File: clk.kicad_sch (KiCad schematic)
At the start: 26 parts, among them U7 SY75602BTWL-TR, U8 SI5338B-B-GM, U9 LMK1C1102DQFT

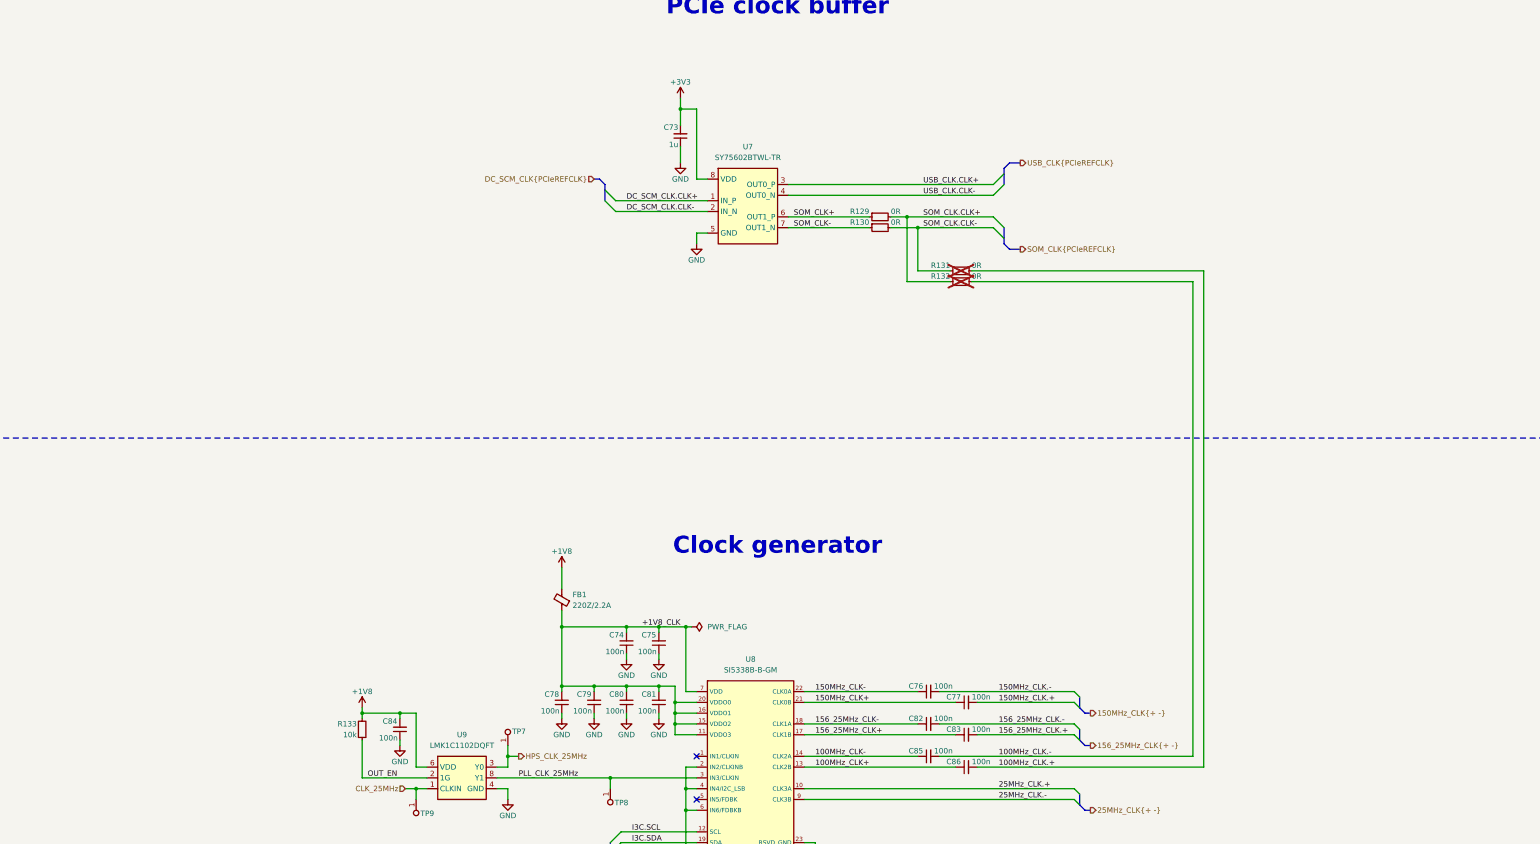
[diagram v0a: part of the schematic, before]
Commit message: [#100687] Reroute PCIE clocks
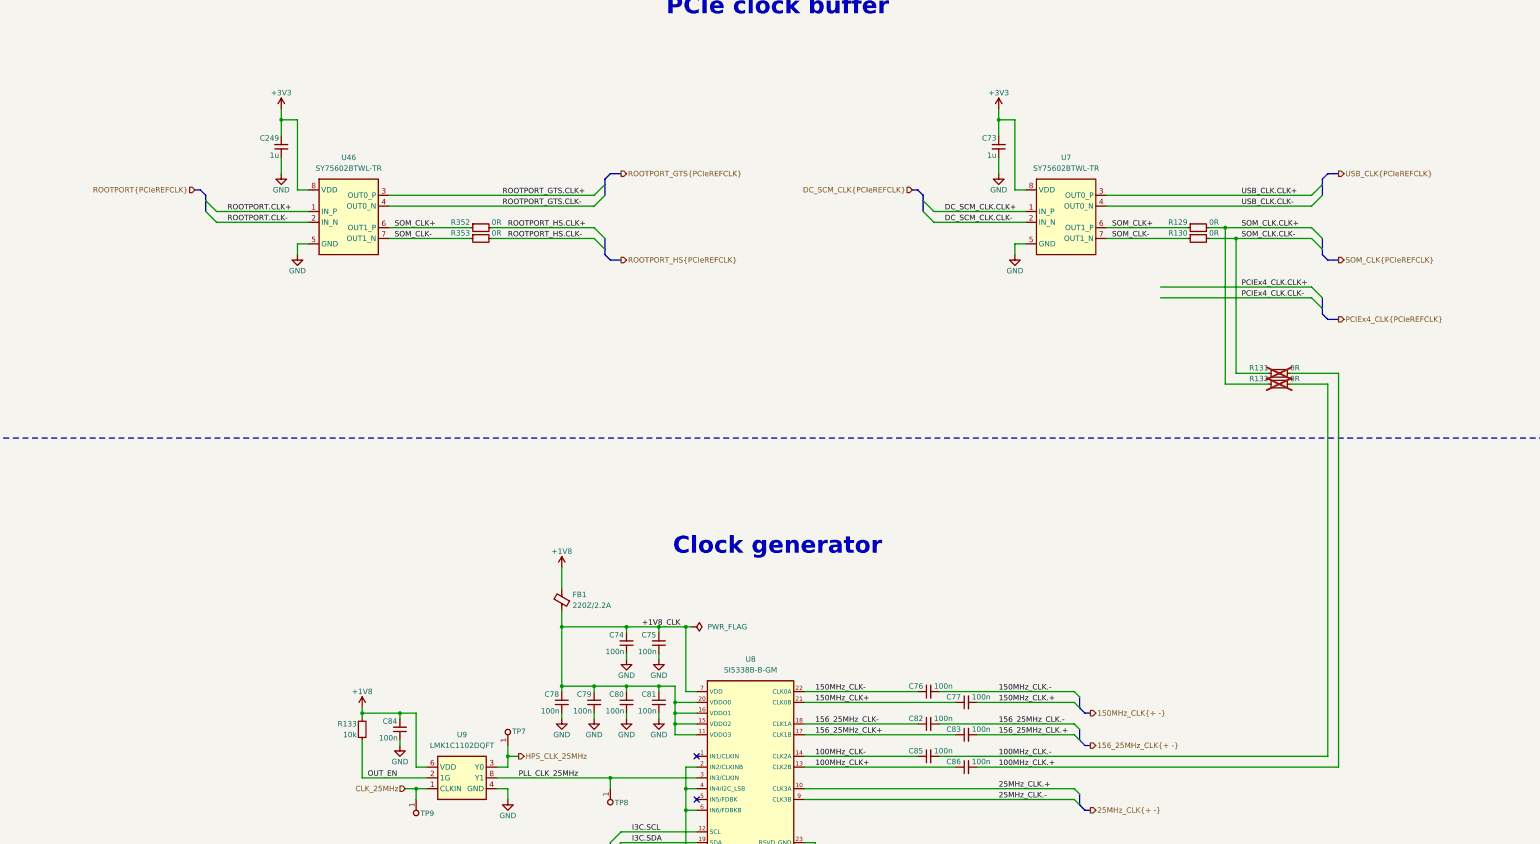
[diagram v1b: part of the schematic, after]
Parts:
- added C249: C_1u_25V_0402, antmicro-footprints:C_0402_1005Metric, symbol antmicroCapacitors0402:C_1u_25V_0402
- added R352, R353: R_0R_0402, antmicro-footprints:R_0402_1005Metric, symbol antmicroResistors0402:R_0R_0402
- added U46: SY75602BTWL-TR, antmicro-footprints:VDFN-8_1.6x1.4mm_P0.4mm, symbol antmicroClockTimingClockGeneratorsPLLsFrequencySynthesizers:SY75602BTWL-TR
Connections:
- net +3V3: now also C249.2, U46.8 (VDD)
- net GND: now also C249.1, U46.5 (GND)
- net SOM_CLK+: now also R352.1, U46.6 (OUT1_P)
- net SOM_CLK-: now also R353.1, U46.7 (OUT1_N)
- new net ROOTPORT.CLK+: U46.1 (IN_P)
- new net ROOTPORT.CLK-: U46.2 (IN_N)
- new net ROOTPORT_GTS.CLK+: U46.3 (OUT0_P)
- new net ROOTPORT_GTS.CLK-: U46.4 (OUT0_N)
- new net ROOTPORT_HS.CLK+: R352.2
- new net ROOTPORT_HS.CLK-: R353.2
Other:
- moved on the sheet: C73, R129, R130, R131, R132, U7

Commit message: [#100687] Add clocks
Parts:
- added C250: C_1u_25V_0402, antmicro-footprints:C_0402_1005Metric, symbol antmicroCapacitors0402:C_1u_25V_0402
- added C251: C_100n_0402, antmicro-footprints:C_0402_1005Metric, symbol antmicroCapacitors0402:C_100n_0402
- added R354, R355, R356, R357, R358, R359: R_0R_0402, antmicro-footprints:R_0402_1005Metric, symbol antmicroResistors0402:R_0R_0402
- added U47: DSC557-0344FI0T, antmicro-footprints:VQFN-14-1EP_3.2x2.5mm_P0.5mm_Layout4x3, symbol antmicroClockTimingRealTimeClocks:DSC557-0344FI0T
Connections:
- net +3V3: now also C250.2, C251.2, U47.1 (OE), U47.12 (VDD1), U47.13 (VDD0)
- net GND: now also C250.1, C251.1, U47.15 (EPAD), U47.4 (VSS)
- net ROOTPORT_GTS.CLK+: now also R354.2, R356.2; no longer U46.3 (OUT0_P)
- net ROOTPORT_GTS.CLK-: now also R355.2, R357.2; no longer U46.4 (OUT0_N)
- net ROOTPORT_HS.CLK+: now also R358.2
- net ROOTPORT_HS.CLK-: now also R359.2
- net SOM_CLK+: no longer R352.1, U46.6 (OUT1_P)
- net SOM_CLK-: no longer R353.1, U46.7 (OUT1_N)
- new net: R356.1, U47.11 (CLK0+)
- new net: R354.1, U46.3 (OUT0_P)
- new net: R352.1, U46.6 (OUT1_P)
- new net: R359.1, U47.9 (CLK1-)
- new net: R357.1, U47.10 (CLK0-)
- new net: U47.14 (NC), U47.2 (NC), U47.3 (NC), U47.5 (NC), U47.6 (NC), U47.7 (NC)
- new net: R358.1, U47.8 (CLK1+)
- new net: R355.1, U46.4 (OUT0_N)
- new net: R353.1, U46.7 (OUT1_N)
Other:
- moved on the sheet: R352, R353

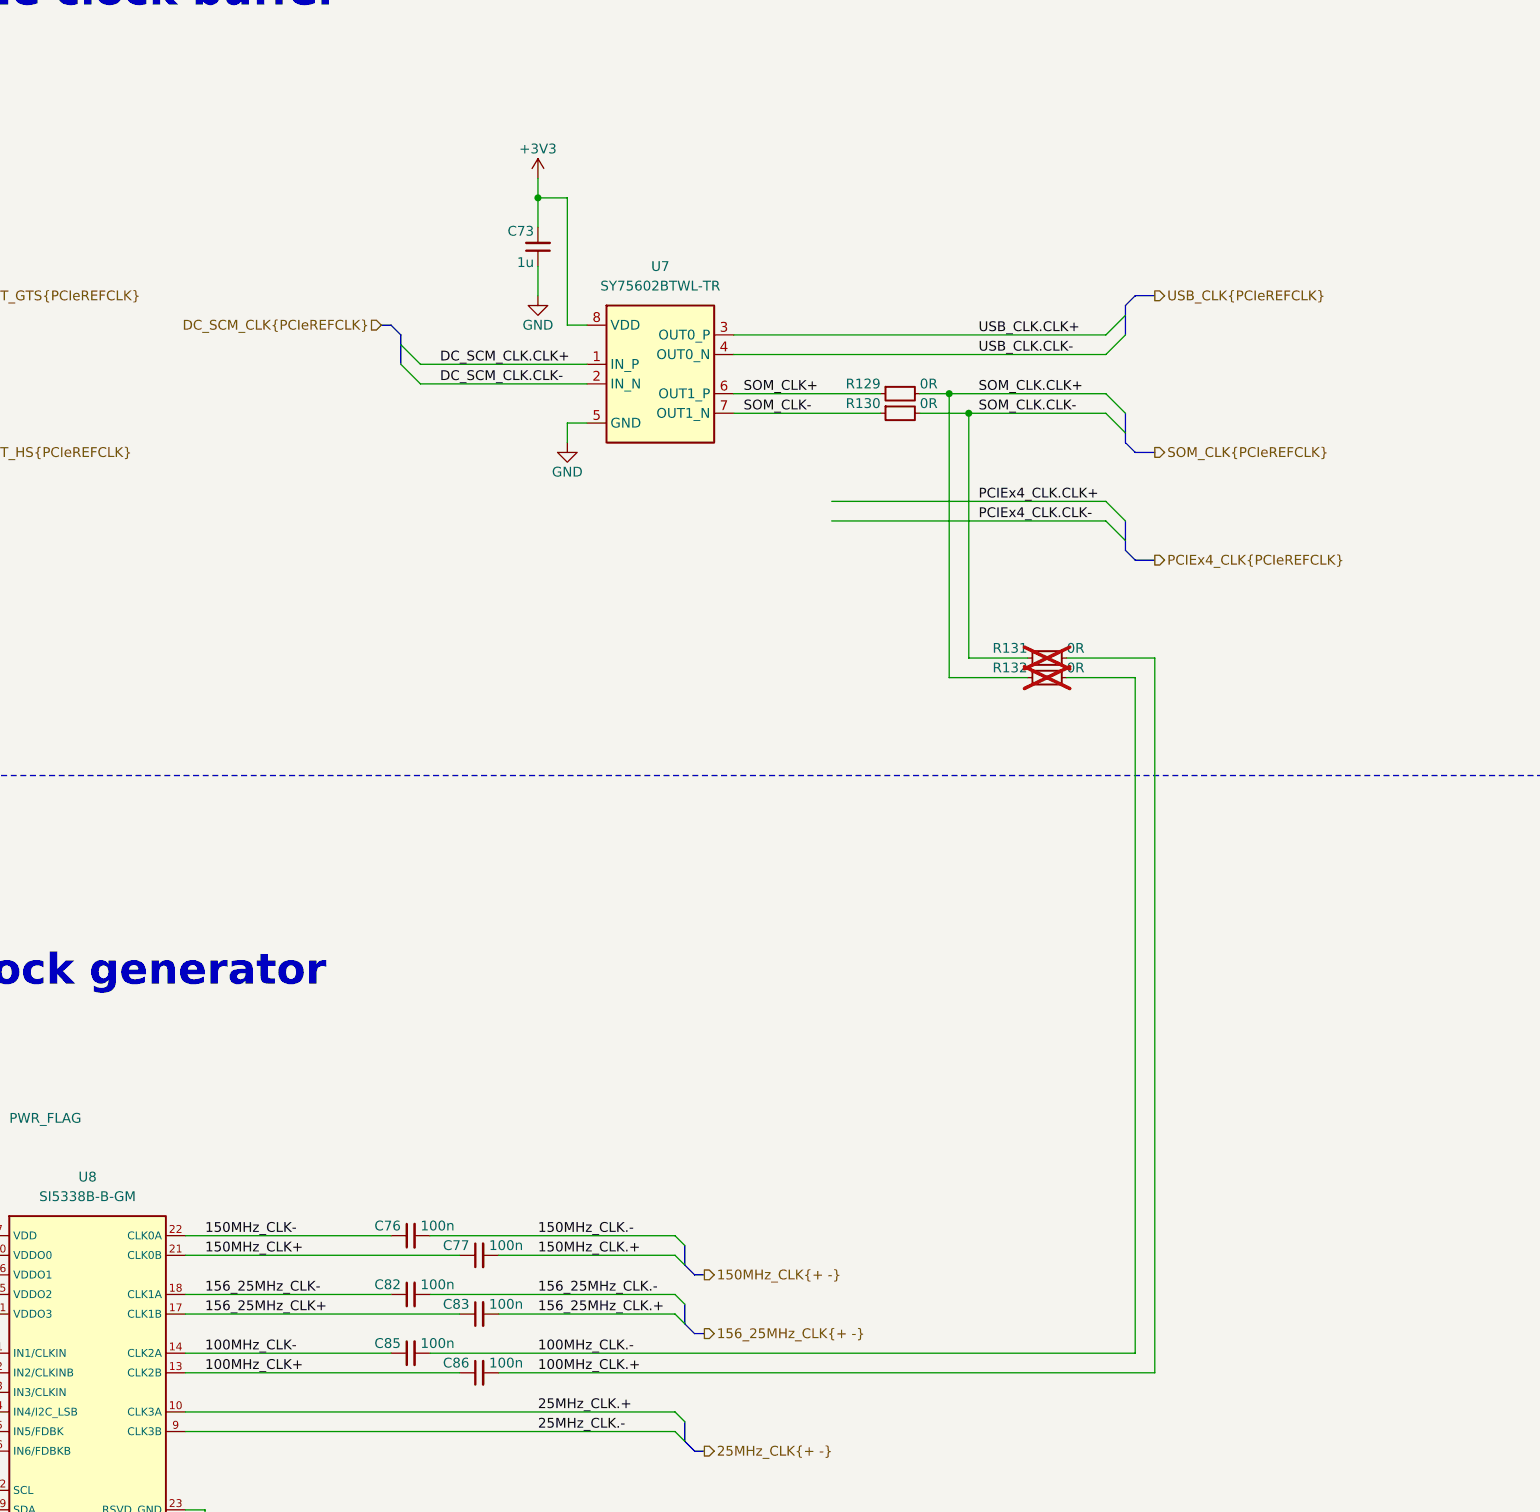
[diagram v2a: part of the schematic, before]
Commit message: [#100687] Update LDO and CLK
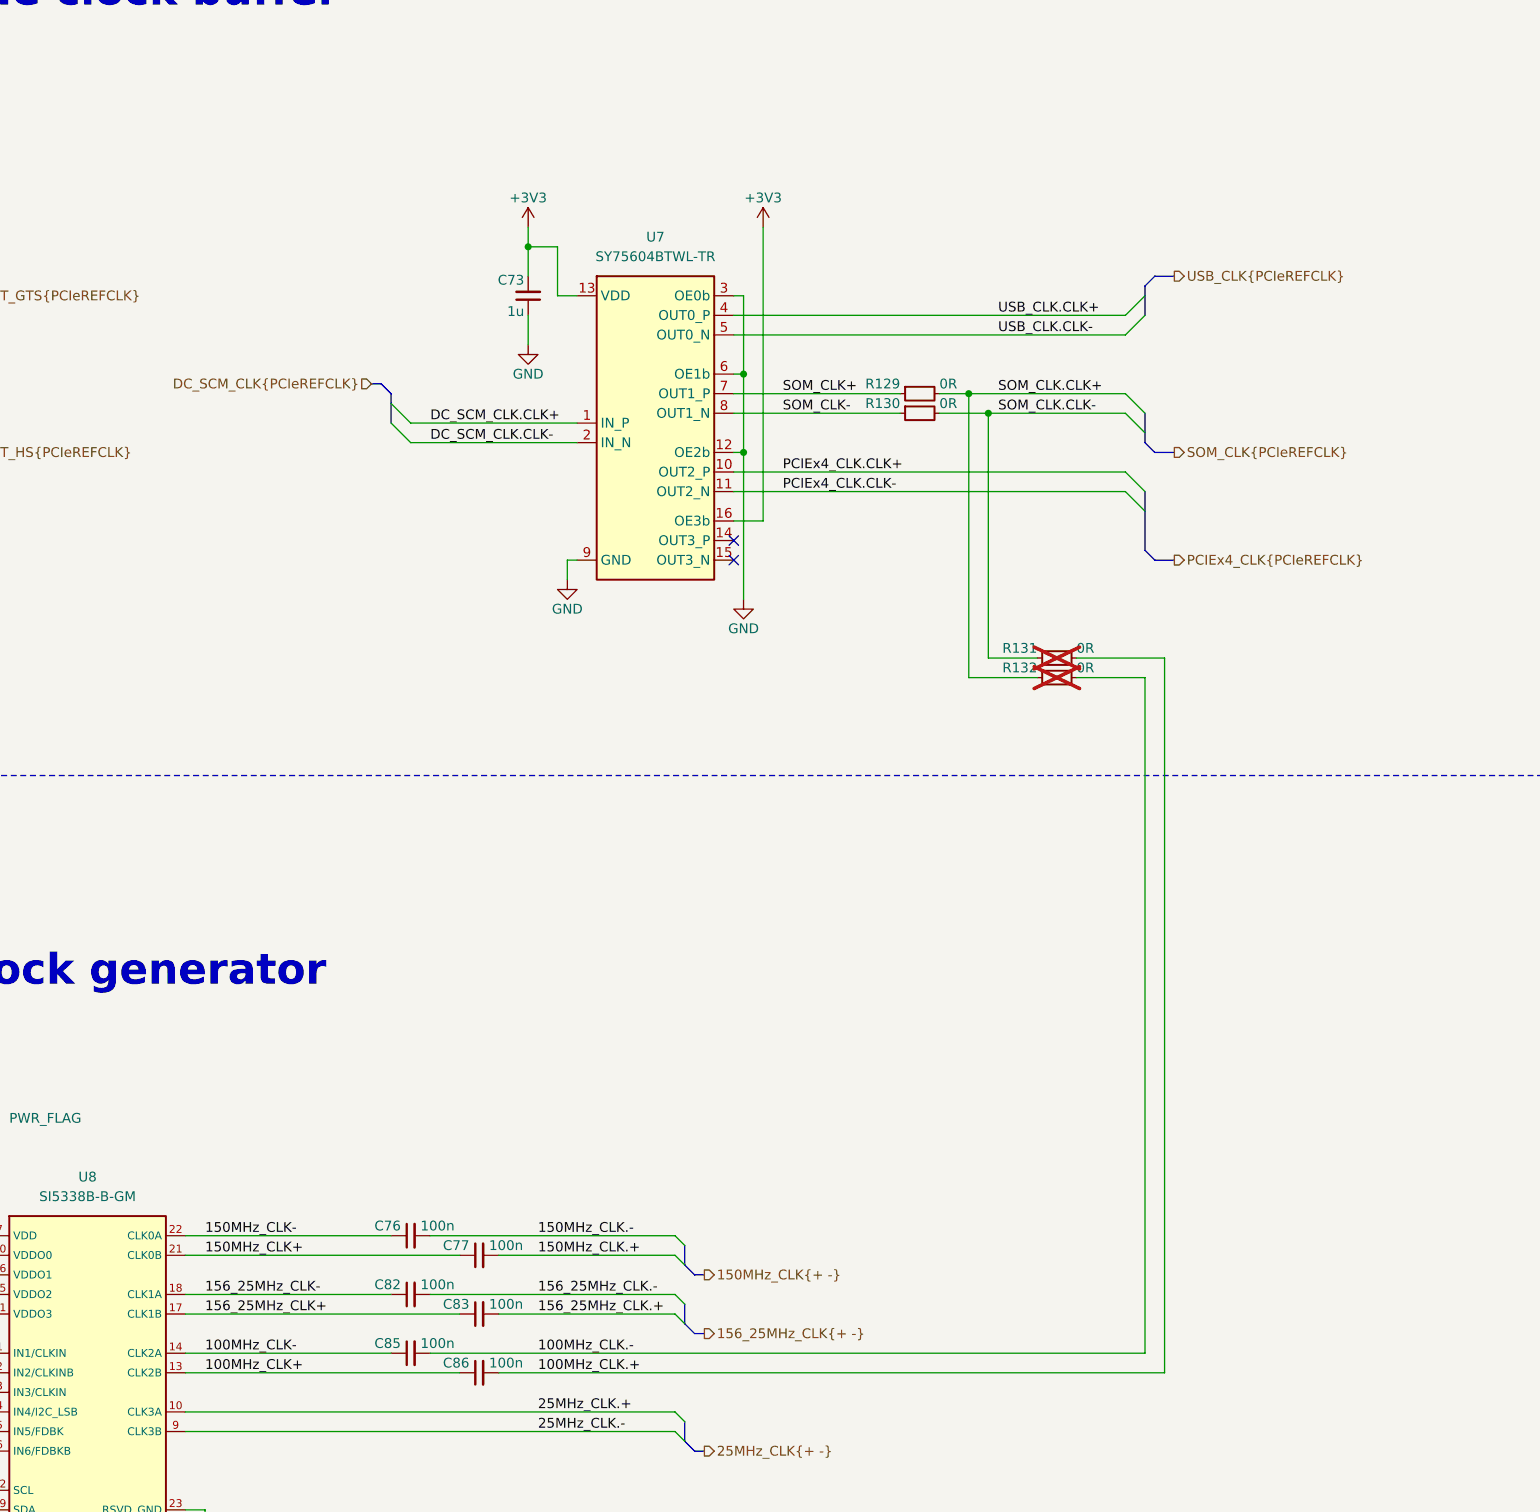
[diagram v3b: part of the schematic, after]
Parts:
- removed U7: SY75602BTWL-TR, antmicro-footprints:VDFN-8_1.6x1.4mm_P0.4mm, symbol antmicroClockTimingClockGeneratorsPLLsFrequencySynthesizers:SY75602BTWL-TR
- added U7: SY75604BTWL-TR, antmicro-footprints:VQFN-16-1EP_3x3mm_P0.5mm_EP1.68x1.68mm, symbol antmicroClockTimingClockGeneratorsPLLsFrequencySynthesizers:SY75604BTWL-TR_1
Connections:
- net +3V3: now also U7.13 (VDD), U7.16 (OE3b)
- net DC_SCM_CLK.CLK+: now also U7.1 (IN_P)
- net DC_SCM_CLK.CLK-: now also U7.2 (IN_N)
- net GND: now also U7.12 (OE2b), U7.3 (OE0b), U7.6 (OE1b), U7.9 (GND)
- net PCIEx4_CLK.CLK+: now also U7.10 (OUT2_P)
- net PCIEx4_CLK.CLK-: now also U7.11 (OUT2_N)
- net SOM_CLK+: now also U7.7 (OUT1_P)
- net SOM_CLK-: now also U7.8 (OUT1_N)
- net USB_CLK.CLK+: now also U7.4 (OUT0_P)
- net USB_CLK.CLK-: now also U7.5 (OUT0_N)
- no-connect marks 3 -> 5
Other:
- moved on the sheet: C73, R129, R130, R131, R132
